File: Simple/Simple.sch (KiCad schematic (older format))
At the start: 21 parts, among them J1 Conn_01x05_Male, J10 Conn_01x02_Female, J2 Conn_01x05_Male, J3 Conn_01x05_Male, J4 Conn_01x05_Male, J5 Conn_01x05_Male, J6 Conn_01x05_Male, J7 Conn_01x04_Male, J8 Conn_01x04_Male, J9 Conn_01x03_Male, SW1 SW_Push, U1 PowerRegulator, U3 ATtiny814-SS

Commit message: Added notes for things to do on simple uC schematic.
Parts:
- U1: symbol My_custom_simple_lib:PowerRegulator -> Simple-rescue:PowerRegulator-My_custom_simple_lib
- U3: symbol MCU_Microchip_ATtiny:ATtiny814-SS -> Simple-rescue:ATtiny814-SS-MCU_Microchip_ATtiny
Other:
- note added: "== Transceiver notes ==\nTie ~RE~ and DE lines together to \nsingle data direction pin on uC.\nA/B differential line needs to be connected to two connectors.\nAvoid stubs and sharp corners.\nA/B differential pair needs to be \nimpedance controlled to 120 Ohms.\n\nData direction line is common to all\nvariations of this board."
- note added: "Add pullups to 5V for SDA, SCL.\nAlso add 5V <-> 3V3 level shifters."
- note added: "Connect misc. data and interrupt lines to uC."
- note added: "ECHO lines should be connected \nto separate, special I/O ports on \nuC connected to 16-bit timers."
- note added: "Motor connectors need to be changed to \n6-pin with ground channel.\nThis might become a 7-pin connector.\n\nINPUT and SPEED_TRIG lines should be \nseparated b/w motors."
- note added: "Use JST PH 2.0 mm pitch connectors."
- note added: "Verify that fixed 3V3 regulator\nhas same pinout."
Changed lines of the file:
@@
 EESchema Schematic File Version 4
-EELAYER 30 0
+LIBS:Simple-cache
+EELAYER 26 0
 EELAYER END
 $Descr A4 11693 8268
 encoding utf-8
 Sheet 1 1
-Title ""
-Date ""
-Rev ""
-Comp ""
-Comment1 ""
+Title "Simple uC"
+Date "2021-02-12"
+Rev "0.0.1"
+Comp "JHU Deliverbot Project"
+Comment1 "Drafted by Bethany Kemp"
 Comment2 ""
 Comment3 ""
@@
 SCL
 $Comp
-L My_custom_simple_lib:PowerRegulator U1
+L Simple-rescue:PowerRegulator-My_custom_simple_lib U1
 U 1 1 600825A1
 P 4650 2000
@@
 $EndComp
 $Comp
-L MCU_Microchip_ATtiny:ATtiny814-SS U3
+L Simple-rescue:ATtiny814-SS-MCU_Microchip_ATtiny U3
 U 1 1 5FF12ACE
 P 3300 4600
@@
 Text Label 7950 4150 0    50   ~ 0
 3V
-Text Label 7950 5050 0    50   ~ 0
+Text Label 7950 5100 0    50   ~ 0
 3V
 Text Label 7950 5900 0    50   ~ 0
@@
 Wire Wire Line
 	7950 5900 7950 6050
+Text Notes 8750 5550 0    50   ~ 0
+Motor connectors need to be changed to \n6-pin with ground channel.\nThis might become a 7-pin connector.\n\nINPUT and SPEED_TRIG lines should be \nseparated b/w motors.
+Text Notes 4450 3000 0    50   ~ 0
+Verify that fixed 3V3 regulator\nhas same pinout.
+Text Notes 5300 3500 0    50   ~ 0
+Add pullups to 5V for SDA, SCL.\nAlso add 5V <-> 3V3 level shifters.
+Text Notes 1150 6500 0    50   ~ 0
+== Transceiver notes ==\nTie ~RE~ and DE lines together to \nsingle data direction pin on uC.\nA/B differential line needs to be connected to two connectors.\nAvoid stubs and sharp corners.\nA/B differential pair needs to be \nimpedance controlled to 120 Ohms.\n\nData direction line is common to all\nvariations of this board.
+Text Notes 5250 4750 0    50   ~ 0
+Connect misc. data and interrupt lines to uC.
+Text Notes 9750 2750 0    50   ~ 0
+ECHO lines should be connected \nto separate, special I/O ports on \nuC connected to 16-bit timers.
+Text Notes 8200 1750 0    50   ~ 0
+Use JST PH 2.0 mm pitch connectors.
 $EndSCHEMATC

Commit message: transceiver added, along with adressing commented changes in schematic
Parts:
- removed J5, J6: Conn_01x05_Male, symbol Connector:Conn_01x05_Male
- removed R1: 27.5k, Resistor_SMD:R_0603_1608Metric, symbol Device:R_Small_US
- removed R2: 10k, Resistor_SMD:R_0603_1608Metric, symbol Device:R_Small_US
- added C5: 1u, Capacitor_SMD:C_0603_1608Metric, symbol Device:C
- added J11: Motor1, Connector_JST:JST_PH_B7B-PH-K_1x07_P2.00mm_Vertical, symbol Connector:Conn_01x07_Male
- added J12: Motor2, Connector_JST:JST_PH_B7B-PH-K_1x07_P2.00mm_Vertical, symbol Connector:Conn_01x07_Male
- added J5, J6: Conn_01x02_Male, Connector_JST:JST_PH_B2B-PH-K_1x02_P2.00mm_Vertical, symbol Connector:Conn_01x02_Male
- added Q1, Q2: BSS138, Package_TO_SOT_SMD:SOT-23, symbol Transistor_FET:BSS138
- added R5: 120, Resistor_SMD:R_0603_1608Metric, symbol Device:R_Small_US
- added R6, R7: 2k2, Resistor_SMD:R_0603_1608Metric, symbol Device:R_Small_US
- added U2: SP485CN-L_TR, NSOIC-8, symbol 2021-02-20_05-48-50:SP485CN-L_TR
- J1: value Conn_01x05_Male -> IR1; footprint (none) -> Connector_JST:JST_PH_B5B-PH-K_1x05_P2.00mm_Vertical
- J10: footprint (none) -> Connector_JST:JST_PH_B2B-PH-K_1x02_P2.00mm_Vertical
- J2: value Conn_01x05_Male -> IR2; footprint (none) -> Connector_JST:JST_PH_B5B-PH-K_1x05_P2.00mm_Vertical
- J3: value Conn_01x05_Male -> IR3; footprint (none) -> Connector_JST:JST_PH_B5B-PH-K_1x05_P2.00mm_Vertical
- J4: value Conn_01x05_Male -> IR4; footprint (none) -> Connector_JST:JST_PH_B5B-PH-K_1x05_P2.00mm_Vertical
- J7: value Conn_01x04_Male -> Ultra1; footprint (none) -> Connector_JST:JST_PH_B4B-PH-K_1x04_P2.00mm_Vertical
- J8: value Conn_01x04_Male -> Ultra2; footprint (none) -> Connector_JST:JST_PH_B4B-PH-K_1x04_P2.00mm_Vertical
- J9: footprint (none) -> Connector_JST:JST_PH_B3B-PH-K_1x03_P2.00mm_Vertical
- U1: value PowerRegulator -> AP7366; symbol Simple-rescue:PowerRegulator-My_custom_simple_lib -> Simple-rescue:PowerRegulator-My_custom_simple_lib-Simple-rescue
- U3: symbol Simple-rescue:ATtiny814-SS-MCU_Microchip_ATtiny -> Simple-rescue:ATtiny814-SS-MCU_Microchip_ATtiny-Simple-rescue
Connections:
- net labels added: +3V3, A, B, DIR1, DIR2, DataDir, ECHO1, ECHO2, INPUT1, INPUT2, SCL_3V3, SDA_3V3, SPEED1, SPEED2, SensorIO1, SensorIO2, SensorIO3, SensorIO4, SensorIO5, SensorIO6, TRIG1, TRIG2
- net labels removed: 3V, DIR, ECHO, INPUT, SPEED_TRIG
- wire segments 81 -> 153
- no-connect marks 0 -> 1
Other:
- note added: "Output (3V3)"
- note removed: "Output (3V)"
- moved on the sheet: C1, C2, C3, C4, J1, J10, J2, J3, J4, J7, J8, J9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

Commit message: SimpleUC: Update to ATTINY816
Updated symbol and schematic to use the larger version of the chip since
we ran out of pins.
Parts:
- U3: symbol Simple-rescue:ATtiny814-SS-MCU_Microchip_ATtiny-Simple-rescue -> Simple-rescue:ATtiny816-MN
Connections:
- wire segments 153 -> 155
- no-connect marks 1 -> 7
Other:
- moved on the sheet: C3
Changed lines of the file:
@@
 	-1   0    0    -1
 $EndComp
-Text Label 1600 4950 2    50   ~ 0
+Text Label 1700 4950 2    50   ~ 0
 RXD
-Text Label 1600 5050 2    50   ~ 0
+Text Label 1700 5050 2    50   ~ 0
 TXD
-Wire Wire Line
-	2600 4300 2600 4350
-Wire Wire Line
-	2500 4300 2600 4300
 $Comp
 L power:GND #PWR0114
 U 1 1 5FF18DE8
-P 2600 4350
-F 0 "#PWR0114" H 2600 4100 50  0001 C CNN
-F 1 "GND" H 2700 4350 50  0000 C CNN
-F 2 "" H 2600 4350 50  0001 C CNN
-F 3 "" H 2600 4350 50  0001 C CNN
-	1    2600 4350
+P 2500 4350
+F 0 "#PWR0114" H 2500 4100 50  0001 C CNN
+F 1 "GND" H 2600 4350 50  0000 C CNN
+F 2 "" H 2500 4350 50  0001 C CNN
+F 3 "" H 2500 4350 50  0001 C CNN
+	1    2500 4350
 	1    0    0    -1
 $EndComp
@@
 L power:GND #PWR0115
 U 1 1 5FF13A15
-P 2200 5850
-F 0 "#PWR0115" H 2200 5600 50  0001 C CNN
-F 1 "GND" H 2205 5677 50  0000 C CNN
-F 2 "" H 2200 5850 50  0001 C CNN
-F 3 "" H 2200 5850 50  0001 C CNN
-	1    2200 5850
-	1    0    0    -1
-$EndComp
-Text Label 1600 4850 2    50   ~ 0
+P 2300 5900
+F 0 "#PWR0115" H 2300 5650 50  0001 C CNN
+F 1 "GND" H 2305 5727 50  0000 C CNN
+F 2 "" H 2300 5900 50  0001 C CNN
+F 3 "" H 2300 5900 50  0001 C CNN
+	1    2300 5900
+	1    0    0    -1
+$EndComp
+Text Label 1700 4850 2    50   ~ 0
 SDA
-Text Label 1600 4750 2    50   ~ 0
+Text Label 1700 4750 2    50   ~ 0
 SCL
 $Comp
@@
 NoConn ~ 9400 1250
 $Comp
-L Simple-rescue:ATtiny814-SS-MCU_Microchip_ATtiny-Simple-rescue U3
+L Simple-rescue:ATtiny816-MN U3
 U 1 1 5FF12ACE
-P 2200 5150
-F 0 "U3" H 1750 5850 50  0000 C CNN
-F 1 "ATtiny814-SS" H 2200 6389 50  0000 C CNN
-F 2 "Package_SO:SOIC-14_3.9x8.7mm_P1.27mm" H 2200 5150 50  0001 C CIN
-F 3 "http://ww1.microchip.com/downloads/en/DeviceDoc/40001912A.pdf" H 2200 5150 50  0001 C CNN
-	1    2200 5150
-	1    0    0    -1
-$EndComp
-Connection ~ 2200 4300
-Wire Wire Line
-	2200 4300 2200 4450
+P 2300 5150
+F 0 "U3" H 1850 5850 50  0000 C CNN
+F 1 "ATtiny814-SS" H 1850 5750 50  0000 C CNN
+F 2 "Package_SO:SOIC-14_3.9x8.7mm_P1.27mm" H 2300 5150 50  0001 C CIN
+F 3 "http://ww1.microchip.com/downloads/en/DeviceDoc/40001912A.pdf" H 2300 5150 50  0001 C CNN
+	1    2300 5150
+	1    0    0    -1
+$EndComp
 $Comp
 L Device:C C3
 U 1 1 5FF154BD
-P 2350 4300
-F 0 "C3" V 2531 4300 50  0000 C CNN
-F 1 "1u" V 2189 4300 50  0000 C CNN
-F 2 "Capacitor_SMD:C_0603_1608Metric" H 2388 4150 50  0001 C CNN
-F 3 "~" H 2350 4300 50  0001 C CNN
-	1    2350 4300
-	0    1    1    0
+P 2500 4200
+F 0 "C3" H 2700 4250 50  0000 C CNN
+F 1 "1u" H 2700 4150 50  0000 C CNN
+F 2 "Capacitor_SMD:C_0603_1608Metric" H 2538 4050 50  0001 C CNN
+F 3 "~" H 2500 4200 50  0001 C CNN
+	1    2500 4200
+	1    0    0    -1
 $EndComp
 Text Label 5550 4400 3    50   ~ 0
@@
 L power:+5V #PWR0105
 U 1 1 5FF1407B
-P 2200 4200
-F 0 "#PWR0105" H 2200 4050 50  0001 C CNN
-F 1 "+5V" H 2215 4412 50  0000 C CNN
-F 2 "" H 2200 4200 50  0001 C CNN
-F 3 "" H 2200 4200 50  0001 C CNN
-	1    2200 4200
+P 2300 4050
+F 0 "#PWR0105" H 2300 3900 50  0001 C CNN
+F 1 "+5V" H 2315 4262 50  0000 C CNN
+F 2 "" H 2300 4050 50  0001 C CNN
+F 3 "" H 2300 4050 50  0001 C CNN
+	1    2300 4050
 	1    0    0    -1
 $EndComp
 Text Notes 850  3550 0    50   ~ 0
 == Transceiver notes ==\nTie ~RE~ and DE lines together to \nsingle data direction pin on uC.\nA/B differential line needs to be connected to two connectors.\nAvoid stubs and sharp corners.\nA/B differential pair needs to be \nimpedance controlled to 120 Ohms.\n\nData direction line is common to all\nvariations of this board.
-Wire Wire Line
-	2200 4200 2200 4300
 Text Label 6250 2800 0    50   ~ 0
 SCL
@@
 Text Label 4400 1000 0    50   ~ 0
 B
+Wire Wire Line
+	2300 4050 2300 4500
+Wire Wire Line
+	2500 4050 2300 4050
+Connection ~ 2300 4050
+Wire Wire Line
+	1700 4750 1800 4750
+Wire Wire Line
+	1700 4850 1800 4850
+Wire Wire Line
+	1700 4950 1800 4950
+Wire Wire Line
+	1700 5050 1800 5050
+NoConn ~ 1800 5150
+NoConn ~ 1800 5250
+NoConn ~ 1800 5400
+NoConn ~ 1800 5500
+NoConn ~ 1800 5600
+NoConn ~ 1800 5700
 $EndSCHEMATC

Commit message: Added interrupt connection to uC
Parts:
- removed R5: 120, Resistor_SMD:R_0603_1608Metric, symbol Device:R_Small_US
- added J? (x2): Conn_01x03_Male, symbol Connector:Conn_01x03_Male
- U3: value ATtiny814-SS -> ATtiny816-SS; symbol Simple-rescue:ATtiny816-MN -> Simple-rescue:ATtiny816-MN-Simple-rescue
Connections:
- net labels added: Interrupt
- wire segments 155 -> 149
- no-connect marks 7 -> 6
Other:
- moved on the sheet: J5, J6
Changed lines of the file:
@@
 Title "Simple uC"
 Date "2021-02-12"
-Rev "0.0.1"
+Rev "0.0.2"
 Comp "JHU Deliverbot Project"
 Comment1 "Drafted by Bethany Kemp"
@@
 NoConn ~ 9400 1250
 $Comp
-L Simple-rescue:ATtiny816-MN U3
+L Simple-rescue:ATtiny816-MN-Simple-rescue U3
 U 1 1 5FF12ACE
 P 2300 5150
 F 0 "U3" H 1850 5850 50  0000 C CNN
-F 1 "ATtiny814-SS" H 1850 5750 50  0000 C CNN
+F 1 "ATtiny816-SS" H 1850 5750 50  0000 C CNN
 F 2 "Package_SO:SOIC-14_3.9x8.7mm_P1.27mm" H 2300 5150 50  0001 C CIN
 F 3 "http://ww1.microchip.com/downloads/en/DeviceDoc/40001912A.pdf" H 2300 5150 50  0001 C CNN
@@
 Wire Wire Line
 	8550 1050 8300 1050
-Text Label 4450 1650 0    50   ~ 0
+Text Label 4100 1650 0    50   ~ 0
 B
-Text Label 3500 1900 0    50   ~ 0
+Text Label 3000 1850 0    50   ~ 0
 A
-Text Label 4400 900  0    50   ~ 0
+Text Label 4950 800  0    50   ~ 0
 A
-Text Label 3500 1700 0    50   ~ 0
+Text Label 3000 1750 0    50   ~ 0
 B
 Text Label 1250 1950 2    50   ~ 0
@@
 Text Label 1250 1650 2    50   ~ 0
 RXD
-Connection ~ 3300 1900
-Wire Wire Line
-	3300 1900 3500 1900
-Connection ~ 3300 1700
-Wire Wire Line
-	3300 1700 3500 1700
-Wire Wire Line
-	3000 1900 3300 1900
-Wire Wire Line
-	3000 1850 3000 1900
-Wire Wire Line
-	3000 1700 3000 1750
-Wire Wire Line
-	3300 1700 3000 1700
 Wire Wire Line
 	2950 1950 2950 2250
@@
 L Connector:Conn_01x02_Male J5
 U 1 1 60304303
-P 4200 900
-F 0 "J5" H 4308 1081 50  0000 C CNN
-F 1 "Conn_01x02_Male" H 4150 1200 50  0000 C CNN
-F 2 "Connector_JST:JST_PH_B2B-PH-K_1x02_P2.00mm_Vertical" H 4200 900 50  0001 C CNN
-F 3 "~" H 4200 900 50  0001 C CNN
-	1    4200 900
+P 3800 900
+F 0 "J5" H 3908 1081 50  0000 C CNN
+F 1 "Conn_01x02_Male" H 3750 1200 50  0000 C CNN
+F 2 "Connector_JST:JST_PH_B2B-PH-K_1x02_P2.00mm_Vertical" H 3800 900 50  0001 C CNN
+F 3 "~" H 3800 900 50  0001 C CNN
+	1    3800 900
 	1    0    0    -1
 $EndComp
@@
 L Connector:Conn_01x02_Male J6
 U 1 1 603052F1
-P 4250 1550
-F 0 "J6" H 4358 1731 50  0000 C CNN
-F 1 "Conn_01x02_Male" H 4150 1850 50  0000 C CNN
-F 2 "Connector_JST:JST_PH_B2B-PH-K_1x02_P2.00mm_Vertical" H 4250 1550 50  0001 C CNN
-F 3 "~" H 4250 1550 50  0001 C CNN
-	1    4250 1550
-	1    0    0    -1
-$EndComp
-$Comp
-L Device:R_Small_US R5
-U 1 1 6045249B
-P 3300 1800
-F 0 "R5" V 3505 1800 50  0000 C CNN
-F 1 "120" V 3414 1800 50  0000 C CNN
-F 2 "Resistor_SMD:R_0603_1608Metric" H 3300 1800 50  0001 C CNN
-F 3 "~" H 3300 1800 50  0001 C CNN
-	1    3300 1800
+P 3900 1550
+F 0 "J6" H 4008 1731 50  0000 C CNN
+F 1 "Conn_01x02_Male" H 3800 1850 50  0000 C CNN
+F 2 "Connector_JST:JST_PH_B2B-PH-K_1x02_P2.00mm_Vertical" H 3900 1550 50  0001 C CNN
+F 3 "~" H 3900 1550 50  0001 C CNN
+	1    3900 1550
 	1    0    0    -1
 $EndComp
@@
 	1    0    0    -1
 $EndComp
-Text Label 4450 1550 0    50   ~ 0
+Text Label 4100 1550 0    50   ~ 0
 A
-Text Label 4400 1000 0    50   ~ 0
+Text Label 4950 900  0    50   ~ 0
 B
 Wire Wire Line
@@
 Wire Wire Line
 	1700 5050 1800 5050
-NoConn ~ 1800 5150
 NoConn ~ 1800 5250
 NoConn ~ 1800 5400
@@
 NoConn ~ 1800 5600
 NoConn ~ 1800 5700
+$Comp
+L Connector:Conn_01x03_Male J?
+U 1 1 604D4C51
+P 4750 900
+F 0 "J?" H 4858 1181 50  0000 C CNN
+F 1 "Conn_01x03_Male" H 4858 1090 50  0000 C CNN
+F 2 "" H 4750 900 50  0001 C CNN
+F 3 "~" H 4750 900 50  0001 C CNN
+	1    4750 900
+	1    0    0    -1
+$EndComp
+Text Label 5000 1400 0    50   ~ 0
+A
+Text Label 5000 1500 0    50   ~ 0
+B
+$Comp
+L Connector:Conn_01x03_Male J?
+U 1 1 60508E02
+P 4800 1500
+F 0 "J?" H 4908 1781 50  0000 C CNN
+F 1 "Conn_01x03_Male" H 4908 1690 50  0000 C CNN
+F 2 "" H 4800 1500 50  0001 C CNN
+F 3 "~" H 4800 1500 50  0001 C CNN
+	1    4800 1500
+	1    0    0    -1
+$EndComp
+Text Label 4950 1000 0    50   ~ 0
+Interrupt
+Text Label 5000 1600 0    50   ~ 0
+Interrupt
+Text Label 1800 5150 2    50   ~ 0
+Interrupt
 $EndSCHEMATC

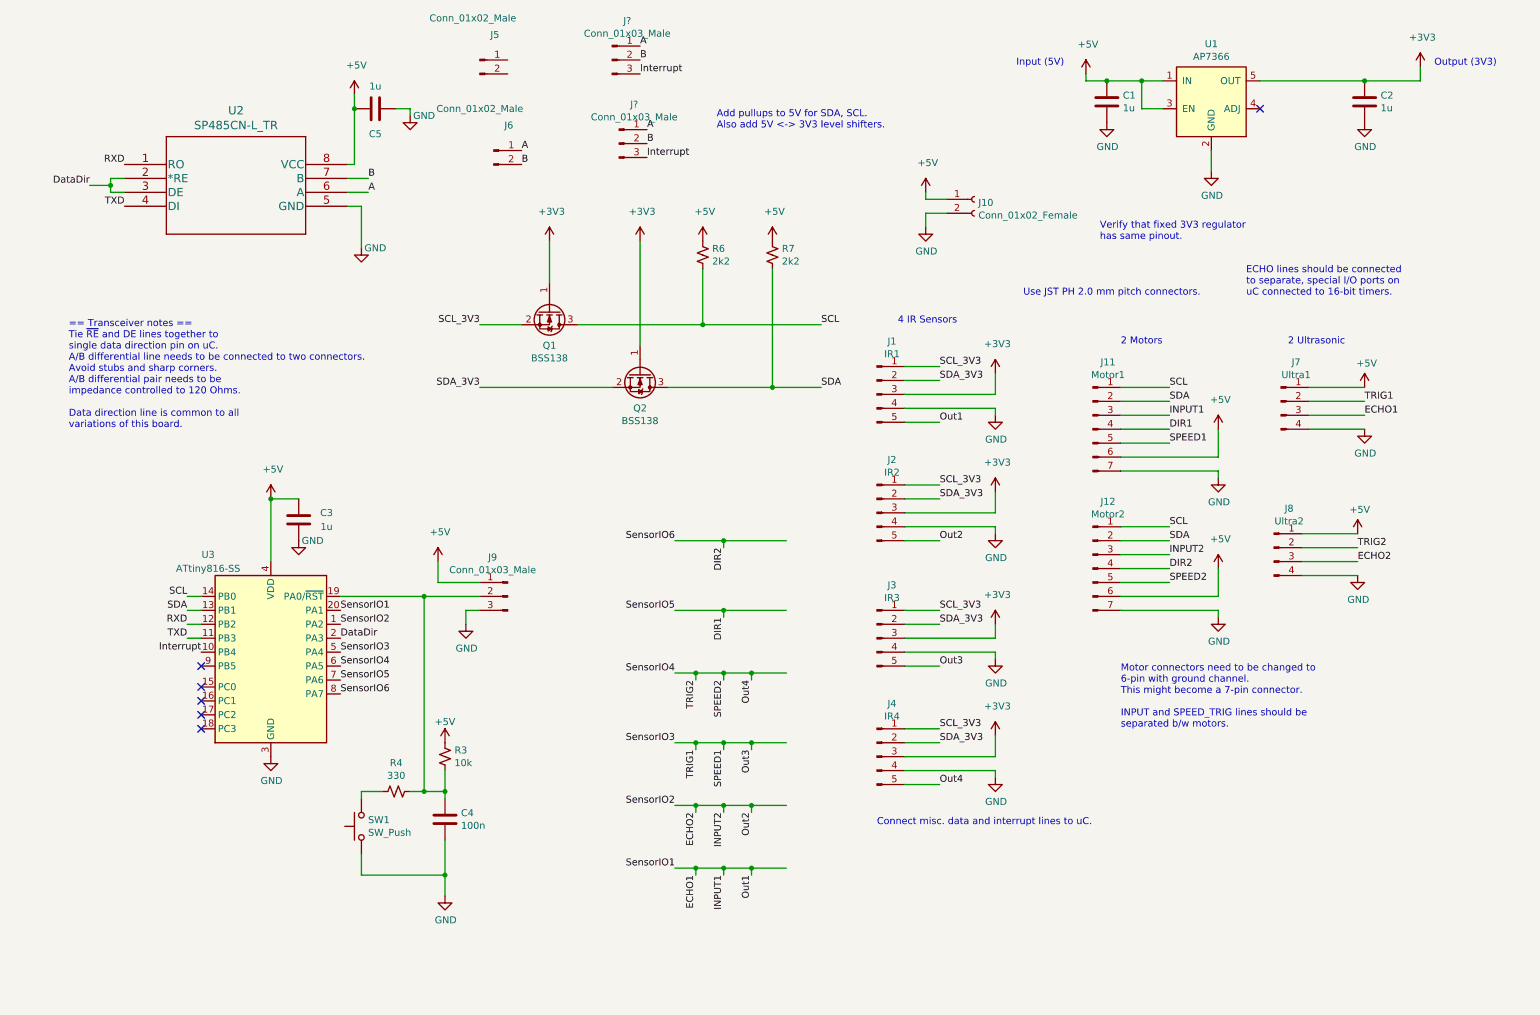
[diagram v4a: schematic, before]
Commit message: Prelayout checkout modifications.  Version pushed to 0.0.3.
Added indicator LEDs, broke out unused pins and extra power pins,
separated data direction pin into two pins --- one for read, one
for write.
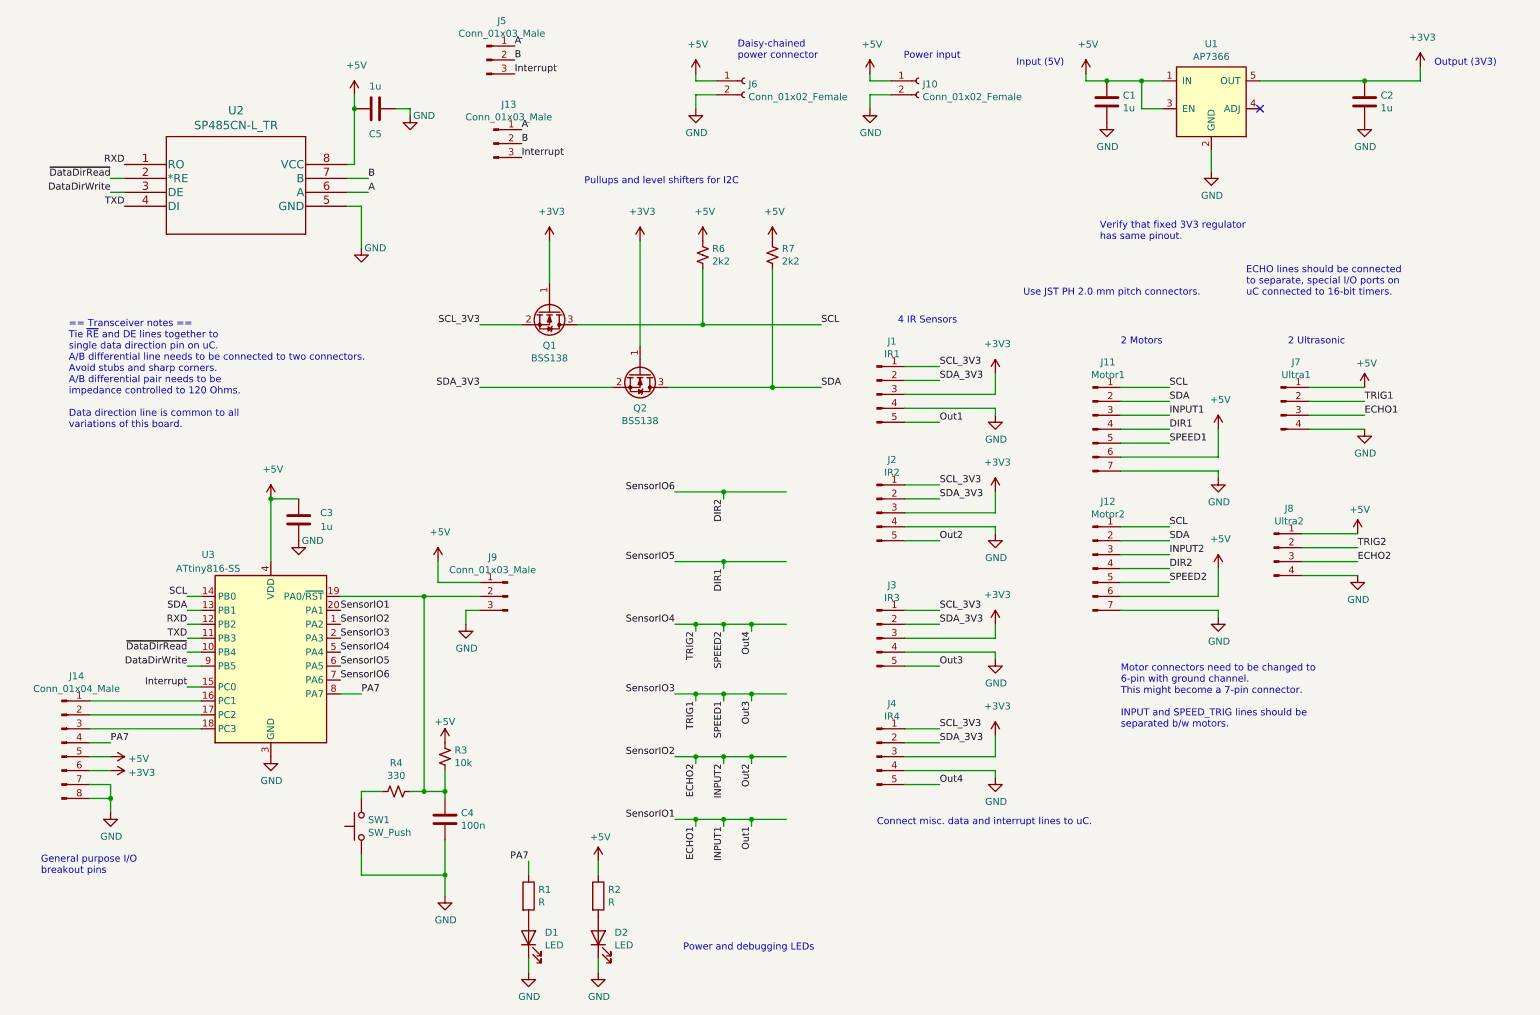
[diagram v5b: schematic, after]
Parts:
- removed J5, J6: Conn_01x02_Male, Connector_JST:JST_PH_B2B-PH-K_1x02_P2.00mm_Vertical, symbol Connector:Conn_01x02_Male
- added D1, D2: LED, LED_SMD:LED_0603_1608Metric, symbol Device:LED
- added J14: Conn_01x04_Male, Connector_JST:JST_PH_B4B-PH-K_1x04_P2.00mm_Vertical, symbol Connector:Conn_01x08_Male
- added J6: Conn_01x02_Female, Connector_JST:JST_PH_B2B-PH-K_1x02_P2.00mm_Vertical, symbol Connector:Conn_01x02_Female
- added R1, R2: R, Resistor_SMD:R_0603_1608Metric, symbol Device:R
- J13, J5: renamed from J?; footprint (none) -> Connector_JST:JST_PH_B3B-PH-K_1x03_P2.00mm_Vertical
- U2: footprint NSOIC-8 -> Package_SO:SOIC-8_3.9x4.9mm_P1.27mm
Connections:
- net labels added: DataDirWrite, PA7, ~DataDirRead
- net labels removed: DataDir
- wire segments 149 -> 168
- no-connect marks 6 -> 1
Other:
- note added: "Daisy-chained \npower connector"
- note added: "General purpose I/O \nbreakout pins"
- note added: "Power and debugging LEDs"
- note added: "Power input"
- note added: "Pullups and level shifters for I2C"
- note removed: "Add pullups to 5V for SDA, SCL.\nAlso add 5V <-> 3V3 level shifters."
- moved on the sheet: J10, J13, J5
